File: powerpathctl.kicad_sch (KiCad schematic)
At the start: 10 parts

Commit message: annotated all schematics, modified ext_devices
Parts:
- gave numbers to parts that had none: 10
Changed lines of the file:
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@@
   (symbol (lib_id "Device:R") (at 194.31 67.31 270) (mirror x) (unit 1)
     (in_bom yes) (on_board yes) (fields_autoplaced)
-    (property "Reference" "R?" (id 0) (at 194.31 61.2902 90))
+    (property "Reference" "R19" (id 0) (at 194.31 61.2902 90))
     (property "Value" "0R" (id 1) (at 194.31 63.8302 90))
     (property "Footprint" "Resistor_SMD:R_0603_1608Metric" (id 2) (at 194.31 69.088 90)
@@
   (symbol (lib_id "Device:D_Schottky_AAK") (at 166.1922 57.912 0) (mirror y) (unit 1)
     (in_bom yes) (on_board yes)
-    (property "Reference" "D?" (id 0) (at 162.9156 52.5018 0))
+    (property "Reference" "D3" (id 0) (at 162.9156 52.5018 0))
     (property "Value" "Schottky SBRT15U50SP5-13" (id 1) (at 169.9768 54.4576 0))
     (property "Footprint" "Diode_SMD:D_PowerDI-5" (id 2) (at 166.8018 59.5884 0)
@@
   (symbol (lib_id "Connector:Conn_01x03_Male") (at 93.345 77.47 0) (unit 1)
     (in_bom yes) (on_board yes)
-    (property "Reference" "J?" (id 0) (at 93.98 69.85 0))
+    (property "Reference" "J4" (id 0) (at 93.98 69.85 0))
     (property "Value" "Conn_01x03_Male_BAT_PWR" (id 1) (at 93.9546 71.9074 0))
     (property "Footprint" "Connector_AMASS:AMASS_MR30PW-M_1x03_P3.50mm_Horizontal" (id 2) (at 93.345 77.47 0)
@@
   (symbol (lib_id "Device:R") (at 114.3 74.93 270) (mirror x) (unit 1)
     (in_bom yes) (on_board yes)
-    (property "Reference" "R?" (id 0) (at 114.0206 71.0692 90))
+    (property "Reference" "R18" (id 0) (at 114.0206 71.0692 90))
     (property "Value" "0R" (id 1) (at 114.2238 72.644 90))
     (property "Footprint" "Resistor_SMD:R_0603_1608Metric" (id 2) (at 114.3 76.708 90)
@@
   (symbol (lib_id "LTC4412ES6:LTC4412ES6") (at 127.635 83.185 0) (unit 1)
     (in_bom yes) (on_board yes)
-    (property "Reference" "U?" (id 0) (at 133.477 78.867 0))
+    (property "Reference" "U9" (id 0) (at 133.477 78.867 0))
     (property "Value" "LTC4412ES6" (id 1) (at 133.477 81.407 0))
     (property "Footprint" "Komponendid:TSOT-23_S6" (id 2) (at 120.015 88.011 0)
@@
   (symbol (lib_id "Device:C") (at 189.23 77.47 0) (unit 1)
     (in_bom yes) (on_board yes) (fields_autoplaced)
-    (property "Reference" "C?" (id 0) (at 192.9384 76.1999 0)
+    (property "Reference" "C46" (id 0) (at 192.9384 76.1999 0)
       (effects (font (size 1.27 1.27)) (justify left))
     )
@@
   (symbol (lib_id "Connector:Conn_01x03_Male") (at 125.476 58.9534 0) (unit 1)
     (in_bom yes) (on_board yes)
-    (property "Reference" "J?" (id 0) (at 126.111 51.3334 0))
+    (property "Reference" "J6" (id 0) (at 126.111 51.3334 0))
     (property "Value" "Conn_01x03_Male_BAT_PWR_IN_NUC_DC_IN" (id 1) (at 126.0856 53.3908 0))
     (property "Footprint" "Connector_AMASS:AMASS_MR30PW-M_1x03_P3.50mm_Horizontal" (id 2) (at 125.476 58.9534 0)
@@
   (symbol (lib_id "Connector:Conn_01x06_Male") (at 127.7112 117.729 0) (mirror y) (unit 1)
     (in_bom yes) (on_board yes)
-    (property "Reference" "J?" (id 0) (at 124.5362 106.934 0)
+    (property "Reference" "J7" (id 0) (at 124.5362 106.934 0)
       (effects (font (size 1.27 1.27)) (justify right))
     )
@@
   (symbol (lib_id "SI7149ADP-T1-GE3:SI7149ADP-T1-GE3") (at 176.53 67.31 0) (mirror y) (unit 1)
     (in_bom yes) (on_board yes) (fields_autoplaced)
-    (property "Reference" "Q?" (id 0) (at 163.83 59.8932 0))
+    (property "Reference" "Q1" (id 0) (at 163.83 59.8932 0))
     (property "Value" "SI7149ADP-T1-GE3" (id 1) (at 163.83 62.4332 0))
     (property "Footprint" "Komponendid:POWERPAKSO-8" (id 2) (at 176.53 67.31 0)
@@
   (symbol (lib_name "Conn_01x06_Male_1") (lib_id "Connector:Conn_01x06_Male") (at 103.5304 117.729 0) (unit 1)
     (in_bom yes) (on_board yes) (fields_autoplaced)
-    (property "Reference" "J?" (id 0) (at 104.1654 107.0356 0))
+    (property "Reference" "J5" (id 0) (at 104.1654 107.0356 0))
     (property "Value" "Conn_01x06_Male " (id 1) (at 104.1654 109.5756 0))
     (property "Footprint" "Connector_JST:JST_PH_S6B-PH-K_1x06_P2.00mm_Horizontal" (id 2) (at 103.5304 117.729 0)

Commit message: assigned LCSC fields to components
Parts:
- C46: footprint Capacitor_SMD:C_0603_1608Metric -> Capacitor_SMD:C_1206_3216Metric; LCSC (none) -> C13585
- D3: LCSC (none) -> C211388
- Q1: LCSC (none) -> C554002
- R18, R19: LCSC (none) -> C21189
- U9: LCSC (none) -> C514442
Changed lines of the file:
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@@
       (effects (font (size 1.27 1.27)) hide)
     )
-    (property "Datasheet" "~" (id 3) (at 194.31 67.31 0)
+    (property "Datasheet" "https://datasheet.lcsc.com/lcsc/2206010130_UNI-ROYAL-Uniroyal-Elec-0603WAF0000T5E_C21189.pdf" (id 3) (at 194.31 67.31 0)
+      (effects (font (size 1.27 1.27)) hide)
+    )
+    (property "LCSC" "C21189" (id 4) (at 194.31 67.31 90)
       (effects (font (size 1.27 1.27)) hide)
     )
@@
       (effects (font (size 1.27 1.27)) hide)
     )
-    (property "Datasheet" "https://4donline.ihs.com/images/VipMasterIC/IC/DIOD/DIOD-S-A0001069870/DIOD-S-A0001069870-1.pdf?hkey=6D3A4C79FDBF58556ACFDE234799DDF0" (id 3) (at 166.1922 57.912 0)
+    (property "Datasheet" "https://datasheet.lcsc.com/lcsc/1806121150_Diodes-Incorporated-SBRT15U50SP5-13_C211388.pdf" (id 3) (at 166.1922 57.912 0)
+      (effects (font (size 1.27 1.27)) hide)
+    )
+    (property "LCSC" "C211388" (id 4) (at 166.1922 57.912 0)
       (effects (font (size 1.27 1.27)) hide)
     )
@@
       (effects (font (size 1.27 1.27)) hide)
     )
-    (property "Datasheet" "~" (id 3) (at 114.3 74.93 0)
+    (property "Datasheet" "https://datasheet.lcsc.com/lcsc/2206010130_UNI-ROYAL-Uniroyal-Elec-0603WAF0000T5E_C21189.pdf" (id 3) (at 114.3 74.93 0)
+      (effects (font (size 1.27 1.27)) hide)
+    )
+    (property "LCSC" "C21189" (id 4) (at 114.3 74.93 90)
       (effects (font (size 1.27 1.27)) hide)
     )
@@
       (effects (font (size 1.27 1.27)) (justify bottom) hide)
     )
+    (property "LCSC" "C514442" (id 6) (at 127.635 83.185 0)
+      (effects (font (size 1.27 1.27)) hide)
+    )
     (pin "1")
     (pin "2")
@@
       (effects (font (size 1.27 1.27)) (justify left))
     )
-    (property "Footprint" "Capacitor_SMD:C_0603_1608Metric" (id 2) (at 190.1952 81.28 0)
+    (property "Footprint" "Capacitor_SMD:C_1206_3216Metric" (id 2) (at 190.1952 81.28 0)
       (effects (font (size 1.27 1.27)) hide)
     )
-    (property "Datasheet" "~" (id 3) (at 189.23 77.47 0)
+    (property "Datasheet" "https://datasheet.lcsc.com/lcsc/1810221112_Samsung-Electro-Mechanics-CL31A106KBHNNNE_C13585.pdf" (id 3) (at 189.23 77.47 0)
+      (effects (font (size 1.27 1.27)) hide)
+    )
+    (property "LCSC" "C13585" (id 4) (at 189.23 77.47 0)
       (effects (font (size 1.27 1.27)) hide)
     )
@@
       (effects (font (size 1.27 1.27)) (justify bottom) hide)
     )
-    (property "Datasheet" "" (id 3) (at 176.53 67.31 0)
+    (property "Datasheet" "https://datasheet.lcsc.com/lcsc/2011170204_Vishay-Intertech-SI7149ADP-T1-GE3_C554002.pdf" (id 3) (at 176.53 67.31 0)
       (effects (font (size 1.27 1.27)) hide)
     )
+    (property "LCSC" "C554002" (id 10) (at 176.53 67.31 0)
+      (effects (font (size 1.27 1.27)) hide)
+    )

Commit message: fixed footprint assignments in powerpath components
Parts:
- Q1: footprint Komponendid:POWERPAKSO-8 -> Robotont:POWERPAKSO-8
- U9: footprint Komponendid:TSOT-23_S6 -> Robotont:TSOT-23_S6
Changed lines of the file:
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@@
     (property "Reference" "U9" (id 0) (at 133.477 78.867 0))
     (property "Value" "LTC4412ES6" (id 1) (at 133.477 81.407 0))
-    (property "Footprint" "Komponendid:TSOT-23_S6" (id 2) (at 120.015 88.011 0)
+    (property "Footprint" "Robotont:TSOT-23_S6" (id 2) (at 120.015 88.011 0)
       (effects (font (size 1.27 1.27)) (justify bottom) hide)
     )
@@
     (property "Reference" "Q1" (id 0) (at 163.83 59.8932 0))
     (property "Value" "SI7149ADP-T1-GE3" (id 1) (at 163.83 62.4332 0))
-    (property "Footprint" "Komponendid:POWERPAKSO-8" (id 2) (at 176.53 67.31 0)
+    (property "Footprint" "Robotont:POWERPAKSO-8" (id 2) (at 176.53 67.31 0)
       (effects (font (size 1.27 1.27)) (justify bottom) hide)
     )

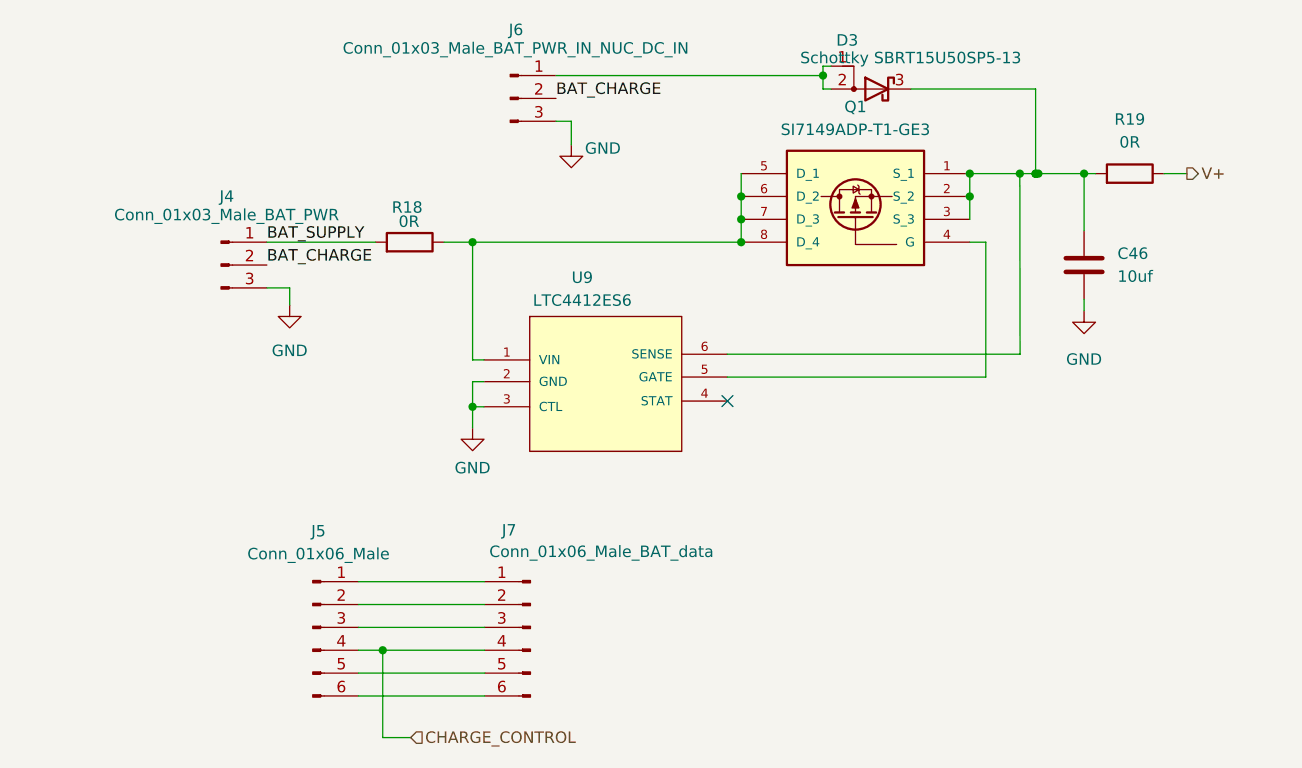
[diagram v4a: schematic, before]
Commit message: assigned names for LEDs; added more footprints; fixed i2c bus connections
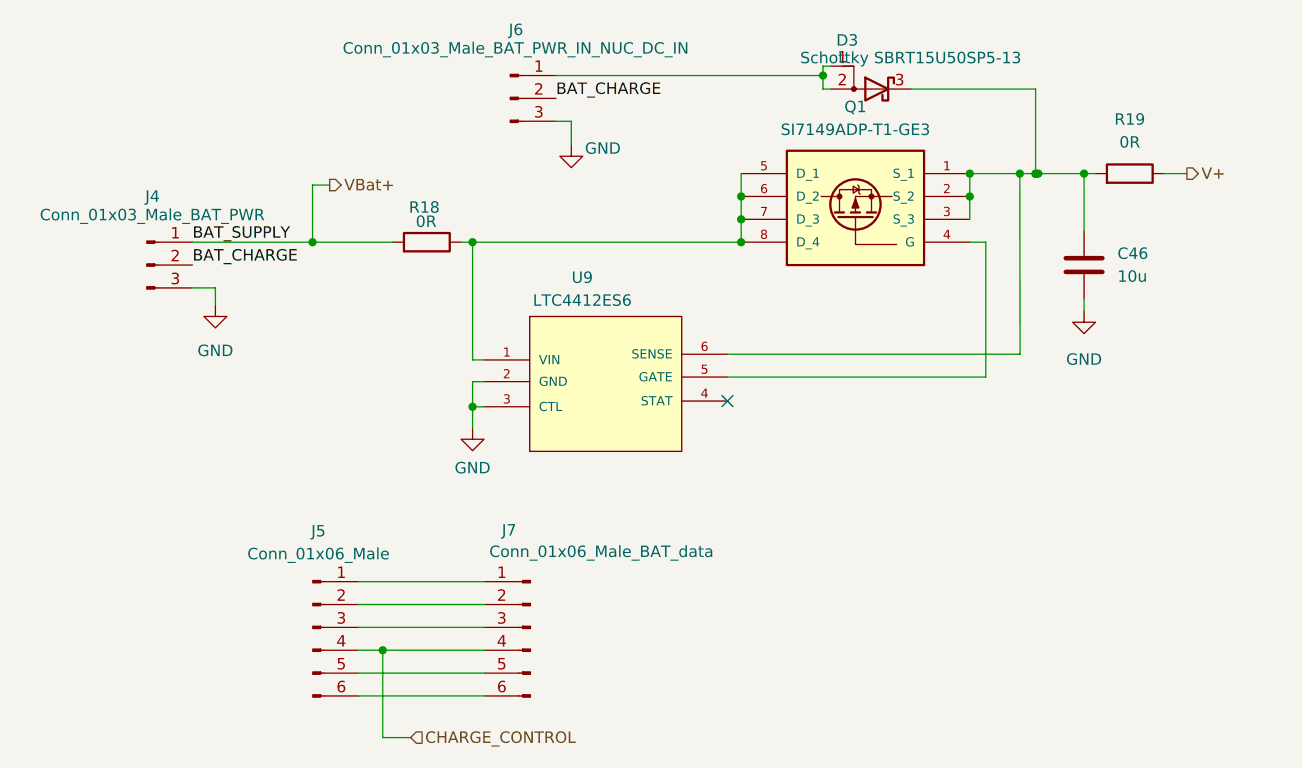
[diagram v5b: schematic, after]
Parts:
- C46: value 10uf -> 10u
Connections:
- net BAT_SUPPLY renamed VBat+
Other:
- moved on the sheet: J4, R18
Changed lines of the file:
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@@
   (junction (at 160.2232 56.4134) (diameter 0) (color 0 0 0 0)
+  )
+  (junction (at 103.505 74.93) (diameter 0) (color 0 0 0 0)
   )
   (junction (at 182.0926 67.31) (diameter 0) (color 0 0 0 0)
@@
     (stroke (width 0) (type default) (color 0 0 0 0))
   )
-  (wire (pts (xy 98.425 74.93) (xy 110.49 74.93))
+  (wire (pts (xy 90.17 74.93) (xy 103.505 74.93))
     (stroke (width 0) (type default) (color 0 0 0 0))
   )
@@
     (stroke (width 0) (type default) (color 0 0 0 0))
   )
-  (wire (pts (xy 98.425 80.01) (xy 100.965 80.01))
+  (wire (pts (xy 90.17 80.01) (xy 92.71 80.01))
     (stroke (width 0) (type default) (color 0 0 0 0))
   )
@@
     (stroke (width 0) (type default) (color 0 0 0 0))
   )
-  (wire (pts (xy 118.11 74.93) (xy 121.285 74.93))
+  (wire (pts (xy 120.015 74.93) (xy 121.285 74.93))
+    (stroke (width 0) (type default) (color 0 0 0 0))
+  )
+  (wire (pts (xy 105.41 68.58) (xy 103.505 68.58))
     (stroke (width 0) (type default) (color 0 0 0 0))
   )
@@
     (stroke (width 0) (type default) (color 0 0 0 0))
   )
+  (wire (pts (xy 103.505 68.58) (xy 103.505 74.93))
+    (stroke (width 0) (type default) (color 0 0 0 0))
+  )
   (wire (pts (xy 149.606 87.376) (xy 182.118 87.376))
     (stroke (width 0) (type default) (color 0 0 0 0))
@@
     (stroke (width 0) (type default) (color 0 0 0 0))
   )
+  (wire (pts (xy 103.505 74.93) (xy 112.395 74.93))
+    (stroke (width 0) (type default) (color 0 0 0 0))
+  )
   (wire (pts (xy 111.3028 120.269) (xy 111.3028 129.9718))
     (stroke (width 0) (type default) (color 0 0 0 0))
@@
     (stroke (width 0) (type default) (color 0 0 0 0))
   )
-  (wire (pts (xy 100.965 80.01) (xy 100.965 81.915))
+  (wire (pts (xy 92.71 80.01) (xy 92.71 81.915))
     (stroke (width 0) (type default) (color 0 0 0 0))
   )
@@
     (stroke (width 0) (type default) (color 0 0 0 0))
   )
-  (label "BAT_CHARGE" (at 98.425 77.47 0)
+  (label "BAT_CHARGE" (at 90.17 77.47 0)
     (effects (font (size 1.27 1.27)) (justify left bottom))
   )
@@
     (effects (font (size 1.27 1.27)) (justify left bottom))
   )
-  (label "BAT_SUPPLY" (at 98.425 74.93 0)
+  (label "BAT_SUPPLY" (at 90.17 74.93 0)
     (effects (font (size 1.27 1.27)) (justify left bottom))
   )
@@
   )
   (hierarchical_label "V+" (shape output) (at 200.66 67.31 0)
+    (effects (font (size 1.27 1.27)) (justify left))
+  )
+  (hierarchical_label "VBat+" (shape output) (at 105.41 68.58 0)
     (effects (font (size 1.27 1.27)) (justify left))
   )
@@
     (pin "3")
   )
-  (symbol (lib_id "Connector:Conn_01x03_Male") (at 93.345 77.47 0) (unit 1)
-    (in_bom yes) (on_board yes)
-    (property "Reference" "J4" (id 0) (at 93.98 69.85 0))
-    (property "Value" "Conn_01x03_Male_BAT_PWR" (id 1) (at 93.9546 71.9074 0))
-    (property "Footprint" "Connector_AMASS:AMASS_MR30PW-M_1x03_P3.50mm_Horizontal" (id 2) (at 93.345 77.47 0)
-      (effects (font (size 1.27 1.27)) hide)
-    )
-    (property "Datasheet" "~" (id 3) (at 93.345 77.47 0)
+  (symbol (lib_id "Connector:Conn_01x03_Male") (at 85.09 77.47 0) (unit 1)
+    (in_bom yes) (on_board yes)
+    (property "Reference" "J4" (id 0) (at 85.725 69.85 0))
+    (property "Value" "Conn_01x03_Male_BAT_PWR" (id 1) (at 85.6996 71.9074 0))
+    (property "Footprint" "Connector_AMASS:AMASS_MR30PW-M_1x03_P3.50mm_Horizontal" (id 2) (at 85.09 77.47 0)
+      (effects (font (size 1.27 1.27)) hide)
+    )
+    (property "Datasheet" "~" (id 3) (at 85.09 77.47 0)
       (effects (font (size 1.27 1.27)) hide)
     )
@@
     (pin "3")
   )
-  (symbol (lib_id "power:GND") (at 100.965 81.915 0) (unit 1)
+  (symbol (lib_id "power:GND") (at 92.71 81.915 0) (unit 1)
     (in_bom yes) (on_board yes) (fields_autoplaced)
-    (property "Reference" "#PWR0150" (id 0) (at 100.965 88.265 0)
-      (effects (font (size 1.27 1.27)) hide)
-    )
-    (property "Value" "GND" (id 1) (at 100.965 86.995 0))
-    (property "Footprint" "" (id 2) (at 100.965 81.915 0)
-      (effects (font (size 1.27 1.27)) hide)
-    )
-    (property "Datasheet" "" (id 3) (at 100.965 81.915 0)
-      (effects (font (size 1.27 1.27)) hide)
-    )
-    (pin "1")
-  )
-  (symbol (lib_id "Device:R") (at 114.3 74.93 270) (mirror x) (unit 1)
-    (in_bom yes) (on_board yes)
-    (property "Reference" "R18" (id 0) (at 114.0206 71.0692 90))
-    (property "Value" "0R" (id 1) (at 114.2238 72.644 90))
-    (property "Footprint" "Resistor_SMD:R_0603_1608Metric" (id 2) (at 114.3 76.708 90)
-      (effects (font (size 1.27 1.27)) hide)
-    )
-    (property "Datasheet" "https://datasheet.lcsc.com/lcsc/2206010130_UNI-ROYAL-Uniroyal-Elec-0603WAF0000T5E_C21189.pdf" (id 3) (at 114.3 74.93 0)
-      (effects (font (size 1.27 1.27)) hide)
-    )
-    (property "LCSC" "C21189" (id 4) (at 114.3 74.93 90)
+    (property "Reference" "#PWR0150" (id 0) (at 92.71 88.265 0)
+      (effects (font (size 1.27 1.27)) hide)
+    )
+    (property "Value" "GND" (id 1) (at 92.71 86.995 0))
+    (property "Footprint" "" (id 2) (at 92.71 81.915 0)
+      (effects (font (size 1.27 1.27)) hide)
+    )
+    (property "Datasheet" "" (id 3) (at 92.71 81.915 0)
+      (effects (font (size 1.27 1.27)) hide)
+    )
+    (pin "1")
+  )
+  (symbol (lib_id "Device:R") (at 116.205 74.93 270) (mirror x) (unit 1)
+    (in_bom yes) (on_board yes)
+    (property "Reference" "R18" (id 0) (at 115.9256 71.0692 90))
+    (property "Value" "0R" (id 1) (at 116.1288 72.644 90))
+    (property "Footprint" "Resistor_SMD:R_0603_1608Metric" (id 2) (at 116.205 76.708 90)
+      (effects (font (size 1.27 1.27)) hide)
+    )
+    (property "Datasheet" "https://datasheet.lcsc.com/lcsc/2206010130_UNI-ROYAL-Uniroyal-Elec-0603WAF0000T5E_C21189.pdf" (id 3) (at 116.205 74.93 0)
+      (effects (font (size 1.27 1.27)) hide)
+    )
+    (property "LCSC" "C21189" (id 4) (at 116.205 74.93 90)
       (effects (font (size 1.27 1.27)) hide)
     )
@@
       (effects (font (size 1.27 1.27)) (justify left))
     )
-    (property "Value" "10uf" (id 1) (at 192.9384 78.7399 0)
+    (property "Value" "10u" (id 1) (at 192.9384 78.7399 0)
       (effects (font (size 1.27 1.27)) (justify left))
     )

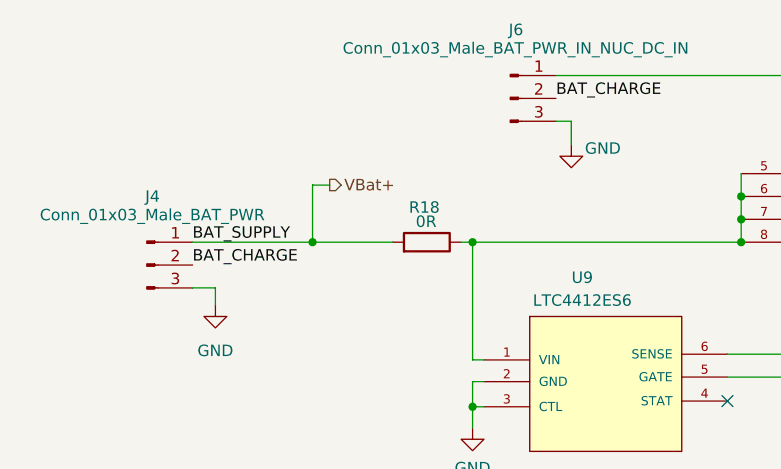
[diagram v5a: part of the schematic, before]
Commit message: reworked USB connections
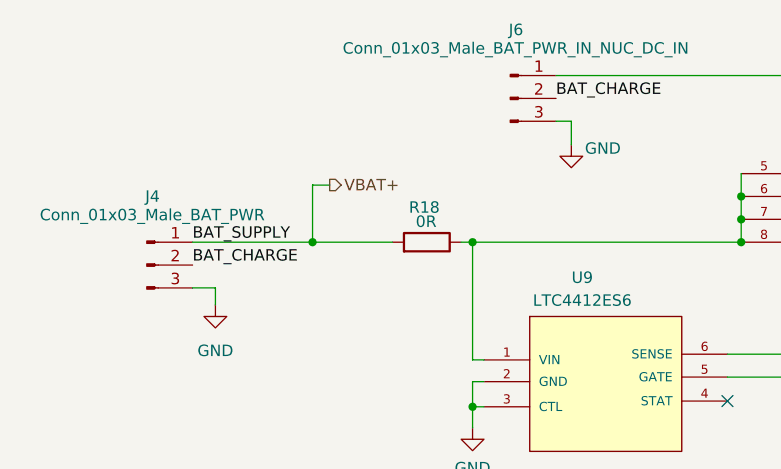
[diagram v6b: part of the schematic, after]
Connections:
- net VBat+ renamed VBAT+
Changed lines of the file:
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@@
     (effects (font (size 1.27 1.27)) (justify left))
   )
-  (hierarchical_label "VBat+" (shape output) (at 105.41 68.58 0)
+  (hierarchical_label "VBAT+" (shape output) (at 105.41 68.58 0)
     (effects (font (size 1.27 1.27)) (justify left))
   )
